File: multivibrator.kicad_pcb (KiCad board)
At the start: 2 copper layers, 43 x 43 mm, 19 parts, among them J1 Conn_01x02_Pin, Q1 2SC1815, Q2 2SC1815

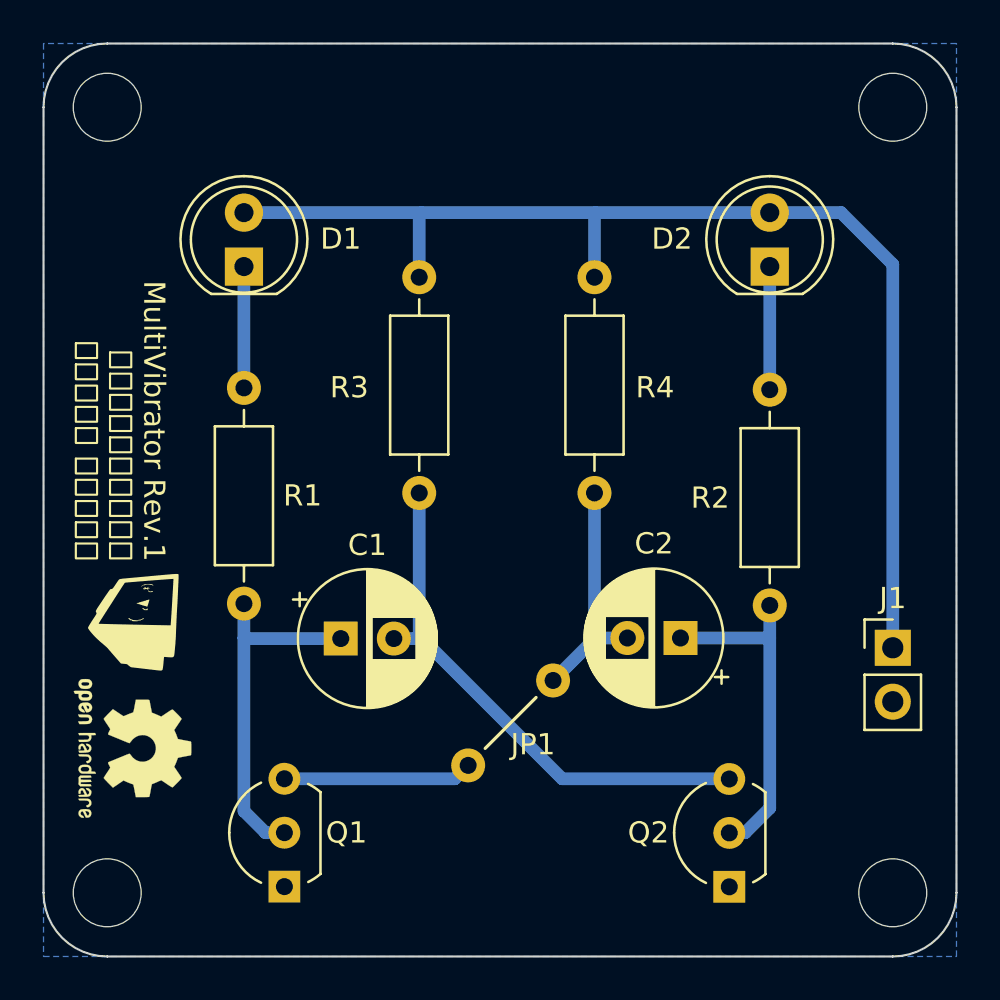
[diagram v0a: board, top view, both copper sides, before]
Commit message: feat: replace footprints of capacitors and connector
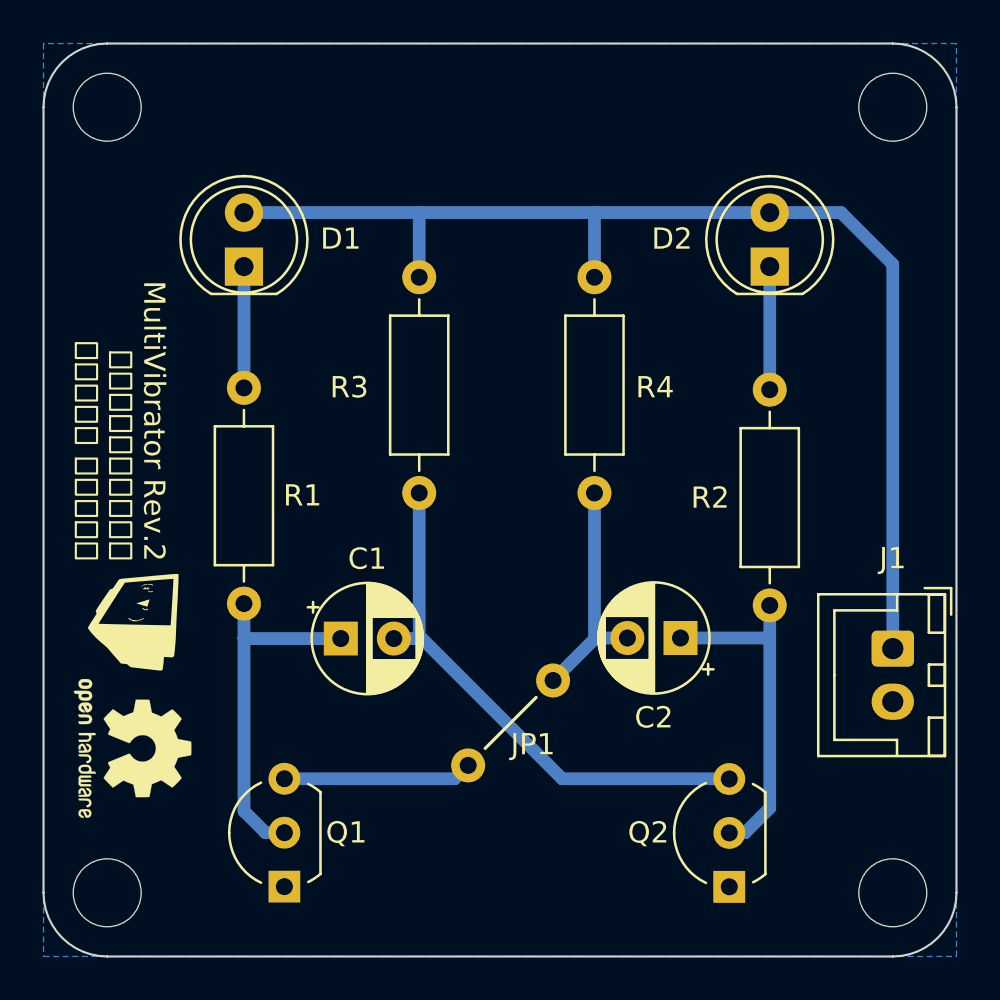
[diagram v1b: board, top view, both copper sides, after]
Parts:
- C1, C2: footprint Capacitor_THT:CP_Radial_D6.3mm_P2.50mm -> Capacitor_THT:CP_Radial_D5.0mm_P2.50mm
- J1: footprint Connector_PinHeader_2.54mm:PinHeader_1x02_P2.54mm_Vertical -> Connector_JST:JST_XH_B2B-XH-A_1x02_P2.50mm_Vertical
- turned J1 to -90 degrees
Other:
- board text added: "MultiVibrator Rev.2 本郷中学校・高等学校 マイコン部 電子工作班"
- board text removed: "MultiVibrator Rev.1 本郷中学校・高等学校 マイコン部 電子工作班"

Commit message: feat: widen jump wire
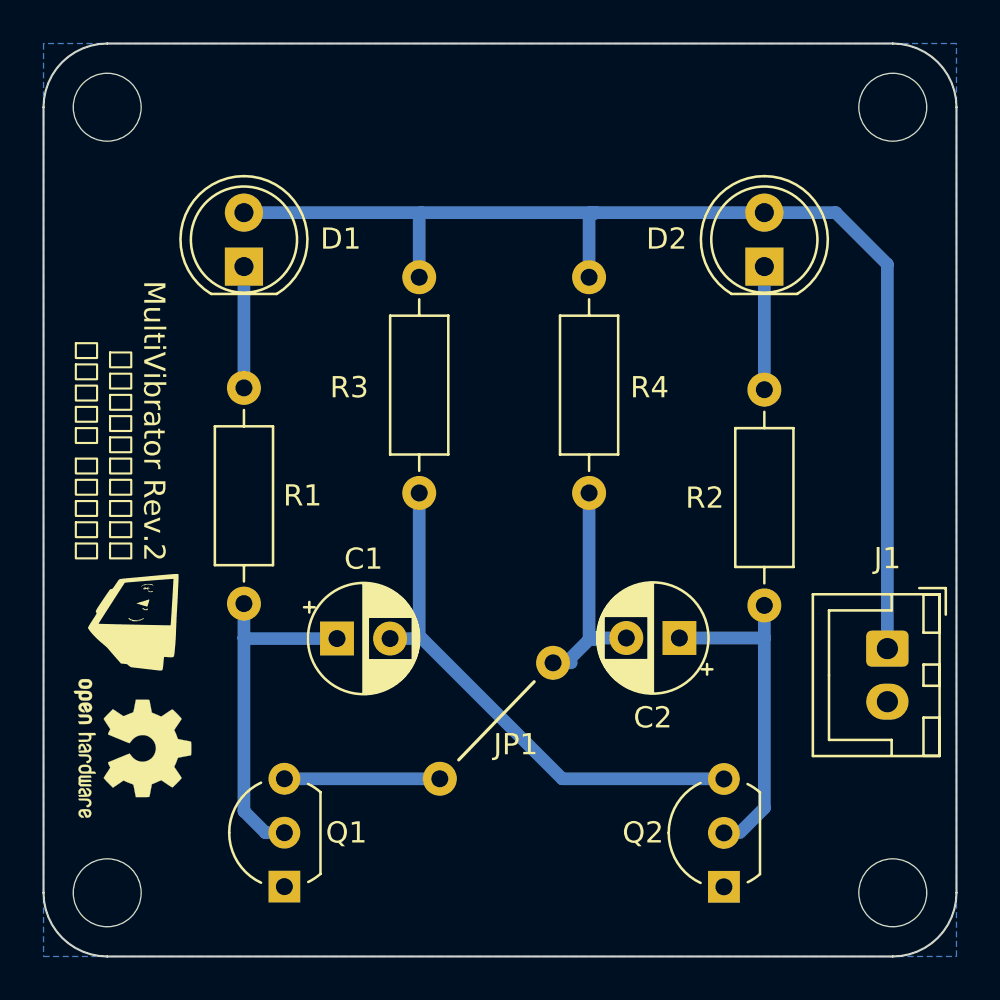
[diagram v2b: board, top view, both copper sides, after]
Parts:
- moved ? 1.48 mm to (100.7, 87.6)
- moved ? 0.83 mm to (106.0, 82.2)
- moved D2 0.25 mm to (116.0, 63.5)
- moved J1 0.25 mm to (121.7, 81.5)
- moved R2 0.25 mm to (116.0, 69.3)
- moved R4 0.25 mm to (107.7, 64.0)
- moved Q2 0.25 mm to (114.0, 92.7)
- moved C1 0.18 mm to (95.8, 81.0)
- moved C2 0.05 mm to (111.9, 81.0)
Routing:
- net Net-(Q1-B): track 20.1 -> 18.2 mm
- net Net-(Q2-C): track 16.1 -> 15.4 mm
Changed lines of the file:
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@@
   (net 8 "GND")
   (footprint "LED_THT:LED_D5.0mm" (layer "F.Cu")
-    (at 116.205 63.505 90)
+    (at 115.951 63.505 90)
     (descr "LED, diameter 5.0mm, 2 pins, http://cdn-reichelt.de/documents/datenblatt/A500/LL-504BC2E-009.pdf")
     (tags "LED diameter 5.0mm 2 pins")
@@
     )
   )
-  (footprint "" locked (layer "F.Cu")
-    (at 106 83)
+  (footprint "" (layer "F.Cu")
+    (at 106 82.169)
     (fp_text reference "" (at 0 0) (layer "F.SilkS")
         (effects (font (size 1.27 1.27) (thickness 0.15)))
@@
   )
   (footprint "Connector_JST:JST_XH_B2B-XH-A_1x02_P2.50mm_Vertical" (layer "F.Cu")
-    (at 122 81.5 -90)
+    (at 121.746 81.5 -90)
     (descr "JST XH series connector, B2B-XH-A (http://www.jst-mfg.com/product/pdf/eng/eXH.pdf), generated with kicad-footprint-generator")
     (tags "connector JST XH vertical")
@@
     )
   )
-  (footprint "" locked (layer "F.Cu")
-    (at 102 87)
+  (footprint "" (layer "F.Cu")
+    (at 100.666 87.63)
     (fp_text reference "" (at 0 0) (layer "F.SilkS")
         (effects (font (size 1.27 1.27) (thickness 0.15)))
@@
   )
   (footprint "Package_TO_SOT_THT:TO-92L_Inline_Wide" (layer "F.Cu")
-    (at 114.3 92.72 90)
+    (at 114.046 92.72 90)
     (descr "TO-92L leads in-line (large body variant of TO-92), also known as TO-226, wide, drill 0.75mm (see https://www.diodes.com/assets/Package-Files/TO92L.pdf and http://www.ti.com/lit/an/snoa059/snoa059.pdf)")
     (tags "TO-92L Inline Wide transistor")
@@
   )
   (footprint "Resistor_THT:R_Axial_DIN0207_L6.3mm_D2.5mm_P10.16mm_Horizontal" (layer "F.Cu")
-    (at 107.95 64.008 -90)
+    (at 107.696 64.008 -90)
     (descr "Resistor, Axial_DIN0207 series, Axial, Horizontal, pin pitch=10.16mm, 0.25W = 1/4W, length*diameter=6.3*2.5mm^2, http://cdn-reichelt.de/documents/datenblatt/B400/1_4W%23YAG.pdf")
     (tags "Resistor Axial_DIN0207 series Axial Horizontal pin pitch 10.16mm 0.25W = 1/4W length 6.3mm diameter 2.5mm")
@@
   )
   (footprint "Capacitor_THT:CP_Radial_D5.0mm_P2.50mm" (layer "F.Cu")
-    (at 96 81.026)
+    (at 95.822888 81.026)
     (descr "CP, Radial series, Radial, pin pitch=2.50mm, , diameter=5mm, Electrolytic Capacitor")
     (tags "CP Radial series Radial pin pitch 2.50mm  diameter 5mm Electrolytic Capacitor")
@@
   )
   (footprint "Resistor_THT:R_Axial_DIN0207_L6.3mm_D2.5mm_P10.16mm_Horizontal" (layer "F.Cu")
-    (at 116.205 69.305 -90)
+    (at 115.951 69.305 -90)
     (descr "Resistor, Axial_DIN0207 series, Axial, Horizontal, pin pitch=10.16mm, 0.25W = 1/4W, length*diameter=6.3*2.5mm^2, http://cdn-reichelt.de/documents/datenblatt/B400/1_4W%23YAG.pdf")
     (tags "Resistor Axial_DIN0207 series Axial Horizontal pin pitch 10.16mm 0.25W = 1/4W length 6.3mm diameter 2.5mm")
@@
   )
   (footprint "Capacitor_THT:CP_Radial_D5.0mm_P2.50mm" (layer "F.Cu")
-    (at 112 81 180)
+    (at 111.949113 81 180)
     (descr "CP, Radial series, Radial, pin pitch=2.50mm, , diameter=5mm, Electrolytic Capacitor")
     (tags "CP Radial series Radial pin pitch 2.50mm  diameter 5mm Electrolytic Capacitor")
@@
     )
   )
-  (gr_line (start 102.8 86.2) (end 105.2 83.8)
+  (gr_line (start 101.555 86.741) (end 105.111 83.058)
     (stroke (width 0.15) (type default)) (layer "F.SilkS"))
   (gr_arc (start 85 96) (mid 82.87868 95.12132) (end 82 93)
@@
   (gr_arc (start 125 93) (mid 124.12132 95.12132) (end 122 96)
     (stroke (width 0.1) (type default)) (layer "Edge.Cuts"))
-  (gr_text "JP1" (at 104 86.6) (layer "F.SilkS")
+  (gr_text "JP1" (at 103.193 86.6) (layer "F.SilkS")
     (effects (font (size 1 1) (thickness 0.15)) (justify left bottom))
   )
@@
   )
   (dimension (type aligned) (layer "Eco1.User")
+    (pts (xy 82 103) (xy 103.5 103))
+    (height -64)
+    (gr_text "21.5000 mm" (at 92.75 37.85) (layer "Eco1.User")
+      (effects (font (size 1 1) (thickness 0.15)))
+    )
+    (format (prefix "") (suffix "") (units 3) (units_format 1) (precision 4))
+    (style (thickness 0.15) (arrow_length 1.27) (text_position_mode 0) (extension_height 0.58642) (extension_offset 0.5) keep_text_aligned)
+  )
+  (dimension (type aligned) (layer "Eco1.User")
     (pts (xy 125 53) (xy 125 96))
     (height 48.292)
@@
   (segment (start 99.695 74.168) (end 99.695 80.921) (width 0.6) (layer "B.Cu") (net 2))
   (segment (start 106.43 87.63) (end 114.3 87.63) (width 0.6) (layer "B.Cu") (net 2))
-  (segment (start 116.205 79.465) (end 116.205 81) (width 0.6) (layer "B.Cu") (net 3))
-  (segment (start 112 81) (end 116.205 81) (width 0.6) (layer "B.Cu") (net 3))
-  (segment (start 116.205 89.011325) (end 116.205 81) (width 0.6) (layer "B.Cu") (net 3))
-  (segment (start 115.046325 90.17) (end 116.205 89.011325) (width 0.6) (layer "B.Cu") (net 3))
-  (segment (start 114.3 90.17) (end 115.046325 90.17) (width 0.6) (layer "B.Cu") (net 3))
-  (segment (start 107.95 81.05) (end 106 83) (width 0.6) (layer "B.Cu") (net 4))
-  (segment (start 107.95 74.168) (end 107.95 81.05) (width 0.6) (layer "B.Cu") (net 4))
+  (segment (start 115.951 79.465) (end 115.951 81) (width 0.6) (layer "B.Cu") (net 3))
+  (segment (start 111.746 81) (end 115.951 81) (width 0.6) (layer "B.Cu") (net 3))
+  (segment (start 115.951 89.011325) (end 115.951 81) (width 0.6) (layer "B.Cu") (net 3))
+  (segment (start 114.792325 90.17) (end 115.951 89.011325) (width 0.6) (layer "B.Cu") (net 3))
+  (segment (start 107.696 74.168) (end 107.696 81.05) (width 0.6) (layer "B.Cu") (net 4))
+  (segment (start 106.6038 82.169) (end 107.696 81.0768) (width 0.6) (layer "B.Cu") (net 4))
+  (segment (start 107.95 81.0768) (end 107.95 81.05) (width 0.6) (layer "B.Cu") (net 4))
   (segment (start 109.5 81) (end 108 81) (width 0.6) (layer "B.Cu") (net 4))
   (segment (start 108 81) (end 107.95 81.05) (width 0.6) (layer "B.Cu") (net 4))
-  (segment (start 101.37 87.63) (end 102 87) (width 0.6) (layer "B.Cu") (net 4))
-  (segment (start 93.345 87.63) (end 101.37 87.63) (width 0.6) (layer "B.Cu") (net 4))
+  (segment (start 100.666 87.63) (end 93.345 87.63) (width 0.6) (layer "B.Cu") (net 4))
+  (segment (start 106 82.169) (end 106.8578 82.169) (width 0.6) (layer "B.Cu") (net 4))
   (segment (start 91.44 63.505) (end 91.44 69.22) (width 0.6) (layer "B.Cu") (net 5))
   (segment (start 99.695 64.008) (end 99.695 61.07) (width 0.6) (layer "B.Cu") (net 6))
   (segment (start 107.95 61.015) (end 108 60.965) (width 0.6) (layer "B.Cu") (net 6))
-  (segment (start 107.95 64.008) (end 107.95 61.015) (width 0.6) (layer "B.Cu") (net 6))
+  (segment (start 107.696 64.008) (end 107.696 61.015) (width 0.6) (layer "B.Cu") (net 6))
   (segment (start 99.695 61.07) (end 99.8 60.965) (width 0.6) (layer "B.Cu") (net 6))
-  (segment (start 122 63.4) (end 119.565 60.965) (width 0.6) (layer "B.Cu") (net 6))
-  (segment (start 119.565 60.965) (end 116.205 60.965) (width 0.6) (layer "B.Cu") (net 6))
-  (segment (start 122 81.46) (end 122 63.4) (width 0.6) (layer "B.Cu") (net 6))
-  (segment (start 108 60.965) (end 116.205 60.965) (width 0.6) (layer "B.Cu") (net 6))
+  (segment (start 121.746 63.4) (end 119.311 60.965) (width 0.6) (layer "B.Cu") (net 6))
+  (segment (start 119.311 60.965) (end 115.951 60.965) (width 0.6) (layer "B.Cu") (net 6))
+  (segment (start 121.746 81.46) (end 121.746 63.4) (width 0.6) (layer "B.Cu") (net 6))
+  (segment (start 107.746 60.965) (end 115.951 60.965) (width 0.6) (layer "B.Cu") (net 6))
   (segment (start 99.8 60.965) (end 108 60.965) (width 0.6) (layer "B.Cu") (net 6))
   (segment (start 91.44 60.965) (end 99.8 60.965) (width 0.6) (layer "B.Cu") (net 6))
-  (segment (start 116.205 63.505) (end 116.205 69.305) (width 0.6) (layer "B.Cu") (net 7))
+  (segment (start 115.951 63.505) (end 115.951 69.305) (width 0.6) (layer "B.Cu") (net 7))
   (zone (net 8) (net_name "GND") (layer "B.Cu") (hatch edge 0.5)
     (connect_pads (clearance 0.5))

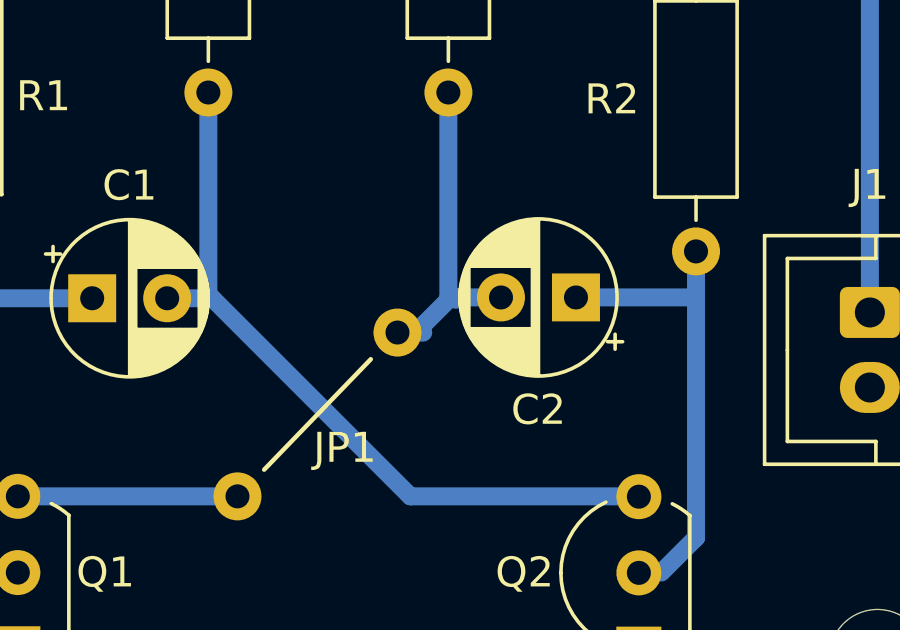
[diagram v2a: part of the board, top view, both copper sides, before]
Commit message: fix: resolve weird path and regenerate gerber
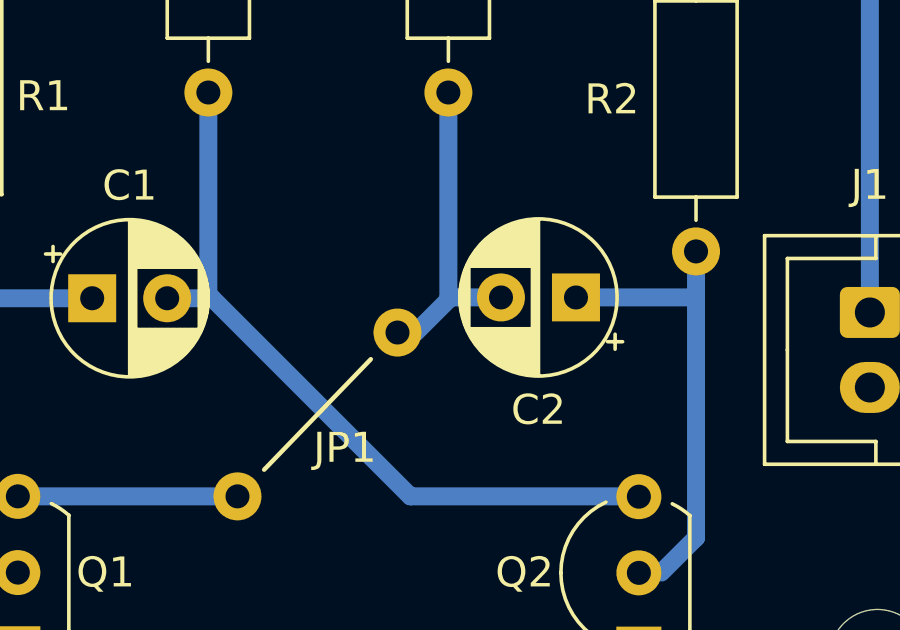
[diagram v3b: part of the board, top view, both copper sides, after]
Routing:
- net Net-(Q1-B): track 18.2 -> 17.5 mm
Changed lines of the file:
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@@
         (effects (font (size 1.27 1.27) (thickness 0.15)))
     )
-    (pad "1" thru_hole oval locked (at 0 0 270) (size 1.6 1.6) (drill 0.8) (layers "*.Cu" "*.Mask")
+    (pad "1" thru_hole oval (at 0 0 270) (size 1.6 1.6) (drill 0.8) (layers "*.Cu" "*.Mask")
       (net 4 "Net-(Q1-B)") (pintype "passive"))
   )
@@
         (effects (font (size 1.27 1.27) (thickness 0.15)))
     )
-    (pad "1" thru_hole oval locked (at 0 0 270) (size 1.6 1.6) (drill 0.8) (layers "*.Cu" "*.Mask")
+    (pad "1" thru_hole oval (at 0 0 270) (size 1.6 1.6) (drill 0.8) (layers "*.Cu" "*.Mask")
       (net 4 "Net-(Q1-B)") (pintype "passive"))
   )
@@
   (segment (start 107.696 74.168) (end 107.696 81.05) (width 0.6) (layer "B.Cu") (net 4))
   (segment (start 106.6038 82.169) (end 107.696 81.0768) (width 0.6) (layer "B.Cu") (net 4))
-  (segment (start 107.95 81.0768) (end 107.95 81.05) (width 0.6) (layer "B.Cu") (net 4))
-  (segment (start 109.5 81) (end 108 81) (width 0.6) (layer "B.Cu") (net 4))
-  (segment (start 108 81) (end 107.95 81.05) (width 0.6) (layer "B.Cu") (net 4))
+  (segment (start 109.449113 81) (end 107.746 81) (width 0.6) (layer "B.Cu") (net 4))
+  (segment (start 107.746 81) (end 107.696 81.05) (width 0.6) (layer "B.Cu") (net 4))
   (segment (start 100.666 87.63) (end 93.345 87.63) (width 0.6) (layer "B.Cu") (net 4))
-  (segment (start 106 82.169) (end 106.8578 82.169) (width 0.6) (layer "B.Cu") (net 4))
   (segment (start 91.44 63.505) (end 91.44 69.22) (width 0.6) (layer "B.Cu") (net 5))
   (segment (start 99.695 64.008) (end 99.695 61.07) (width 0.6) (layer "B.Cu") (net 6))
